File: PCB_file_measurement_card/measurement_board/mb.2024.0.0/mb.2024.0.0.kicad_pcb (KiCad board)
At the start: 2 copper layers, 235 x 124 mm, 85 parts, among them J1 DSP_out_12v_GND, J10 DSP+, J11 Screw_Terminal_VMN, J12 Conn_01x08_Female, J14 Conn_01x02_Female, J15 Conn_01x08_Female, J16 RX_bat, J17 DSP GND, J18 ELEC_M, J19 ELEC_N, J2 DPS5005_input_0_to_50V, J20 shunt +, J21 shunt -, J3 Screw_Terminal_AB, J4 Conn_01x08_Female, J5 Conn_01x04_Female, J6 Conn_01x08_Female, J7 Raspberry_Pi_2_3, J8 Connector_I2C_for_mux_or_tools, J9 TX_bat, K1 G5LE-1, K2 G5LE-1, K3 AQY212EH, K4 AQY212EH, K5 AQY212EH, K6 AQY212EH, Q1 ZVN4206ASTZ, Q2 ZVN4206ASTZ, U1 MCP23008-xP, U2 OP07, U3 24LC02, U4 1115-Adress=0X49, U5 1115-Adress=0X48, U6 OP07, U7 OP07

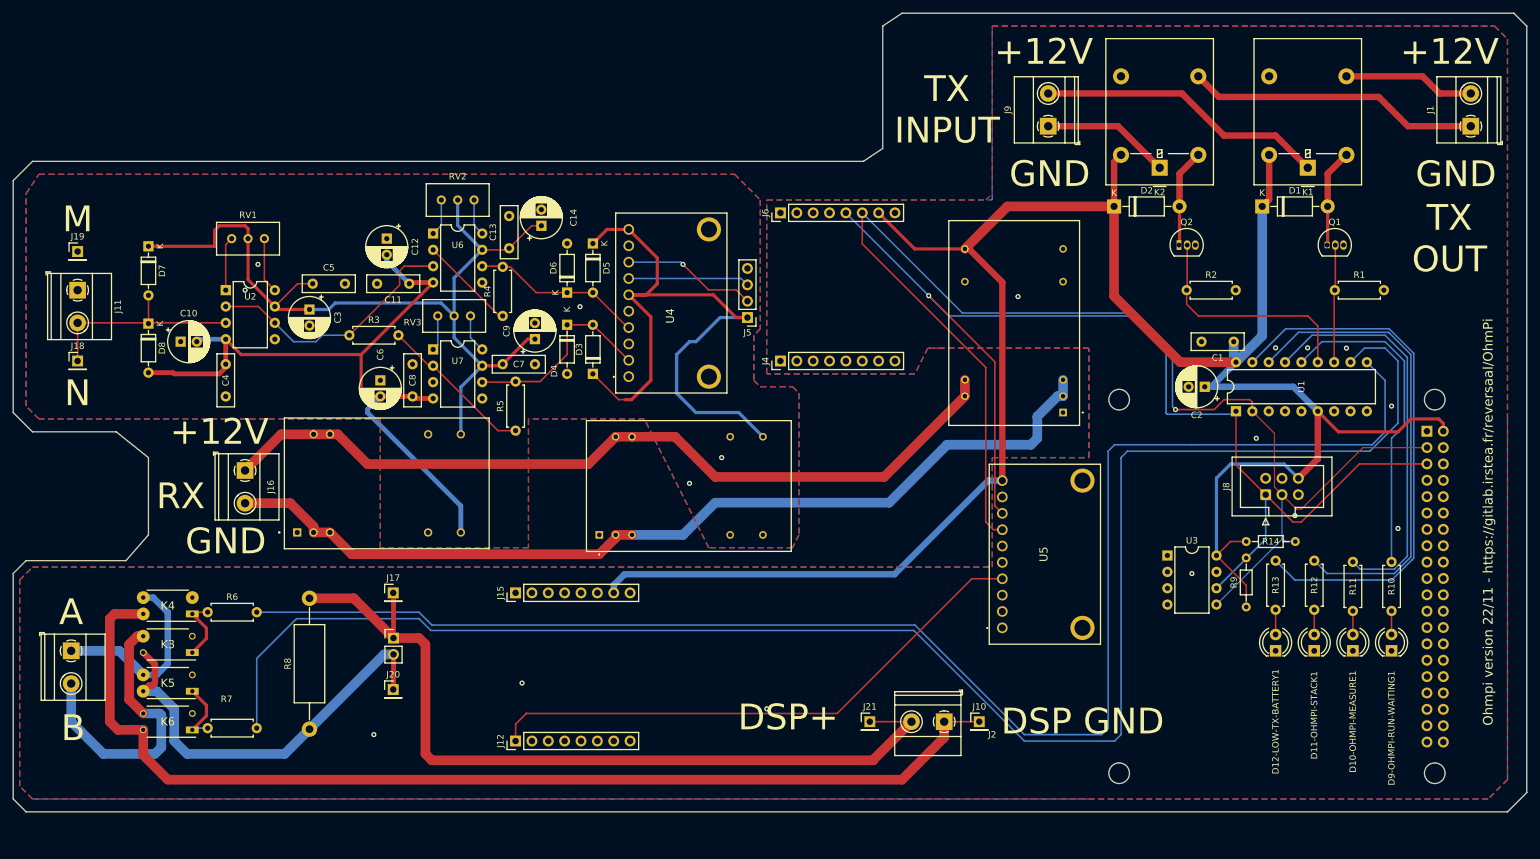
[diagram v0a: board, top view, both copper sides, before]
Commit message: rename file with the tag version
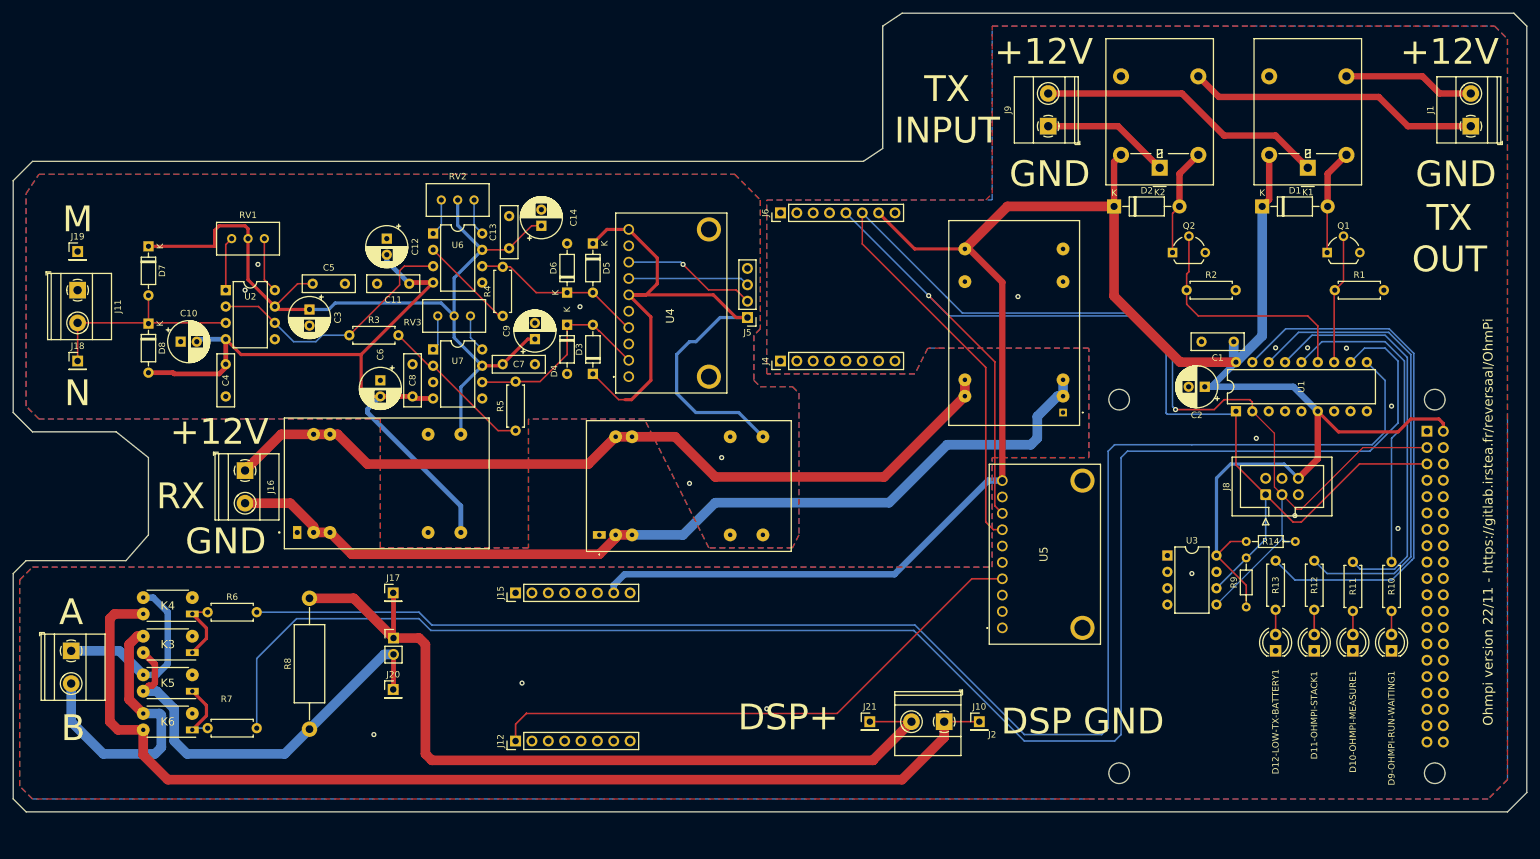
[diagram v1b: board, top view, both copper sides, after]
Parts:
- Q1, Q2: footprint Package_TO_SOT_THT:TO-92L_Inline -> Package_TO_SOT_THT:TO-92L_Wide
- moved Q2 1.53 mm to (207.0, 68.2)
- moved Q1 1.16 mm to (231.0, 68.2)
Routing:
- net GP2: track 18.3 -> 20.2 mm
- net Net-(D2-Pad2): track 15.1 -> 16.8 mm
- net GP3: track 36.6 -> 38.1 mm
- net Net-(D1-Pad2): track 15.1 -> 16.4 mm

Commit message: uptdate version
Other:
- board text added: "Ohmpi version mb.2024.0.0 - https://gitlab.irstea.fr/reversaal/OhmPi"
- board text removed: "Ohmpi version 22/11 - https://gitlab.irstea.fr/reversaal/OhmPi"
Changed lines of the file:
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@@
     (effects (font (size 4 4) (thickness 0.5)))
   )
-  (gr_text "Ohmpi version 22/11 - https://gitlab.irstea.fr/reversaal/OhmPi" (at 256 110 90) (layer "F.SilkS")
+  (gr_text "Ohmpi version mb.2024.0.0 - https://gitlab.irstea.fr/reversaal/OhmPi" (at 256 110 90) (layer "F.SilkS")
     (effects (font (size 1.5 1.5) (thickness 0.3)))
   )

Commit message: update
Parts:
- moved R1 7.85 mm to (240.0, 73.7), turned to 180 degrees
- moved Q1 5.23 mm to (236.2, 68.2), turned to 180 degrees
- moved Q2 5.10 mm to (212.1, 68.2), turned to 180 degrees
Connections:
- Q1 pad 1: Net-(D1-Pad2) -> GNDD
- Q1 pad 3: GNDD -> Net-(D1-Pad2)
- Q2 pad 1: Net-(D2-Pad2) -> GNDD
- Q2 pad 3: GNDD -> Net-(D2-Pad2)
- R1 pad 1: GP2 -> GNDD
- R1 pad 2: GNDD -> GP2
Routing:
- net GP2: track 20.2 -> 15.1 mm
- net GP3: track 38.1 -> 33.5 mm
